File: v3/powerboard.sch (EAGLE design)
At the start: 4 parts, among them U1 TPS63001DRCR

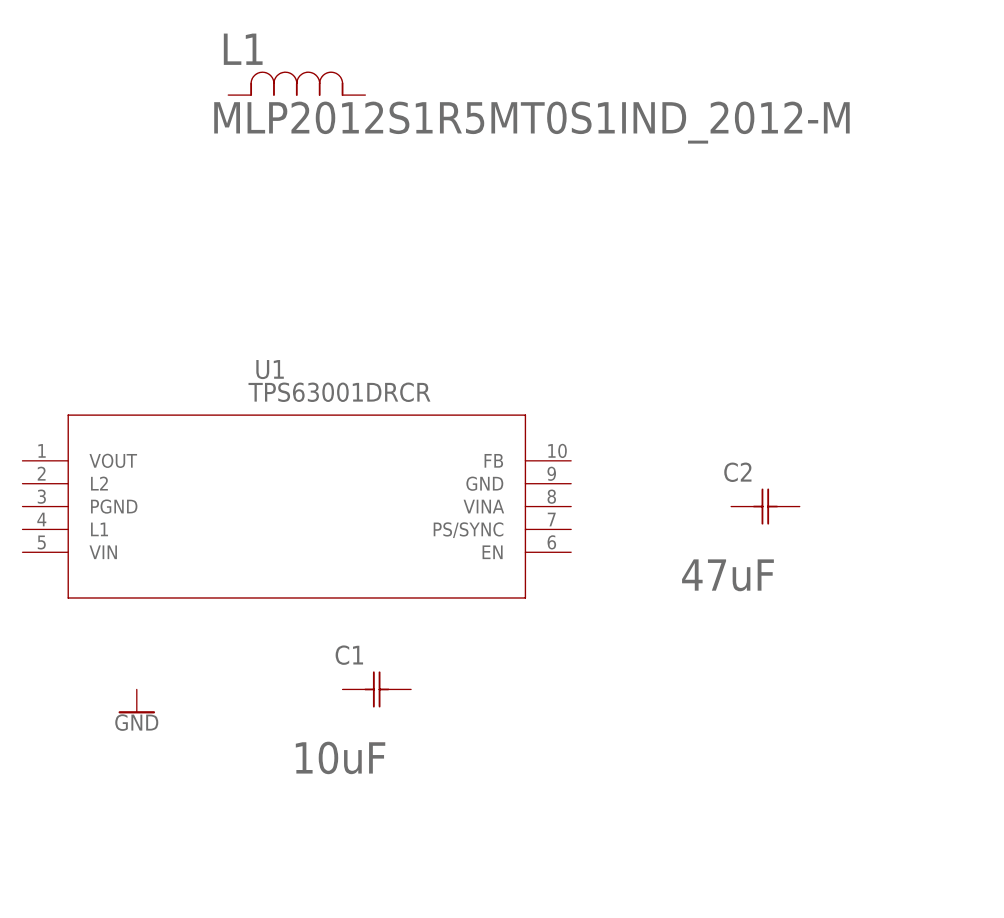
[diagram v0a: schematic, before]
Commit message: Progress on two-rail power supply.
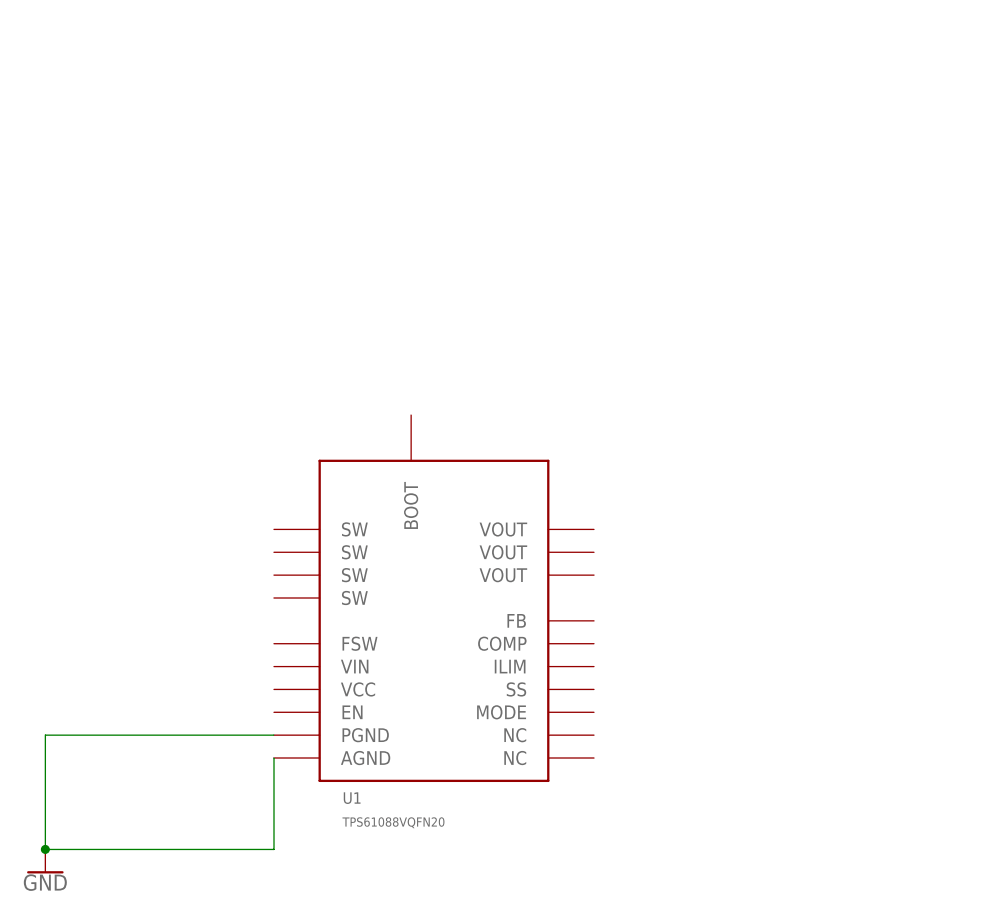
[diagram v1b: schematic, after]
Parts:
- removed C1: 10uF, Murata_By_element14_Batch_1:GRM188R60J106ME47D
- removed C2: 47uF, Murata_By_element14_Batch_1:GRM31MR71E105KA01L
- removed L1: MLP2012S1R5MT0S1IND_2012-M, digikey_2:MLP2012S1R5MT0S1IND_2012-M
- U1: value TPS63001DRCR -> TPS61088VQFN20; device digikey_2:TPS63001DRCR -> digikey:TPS61088VQFN20
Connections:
- new net GND: U1.AGND, U1.PGND
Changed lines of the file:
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@@
 </classes>
 <parts>
-<part name="L1" library="digikey_2" deviceset="MLP2012S1R5MT0S1" device="IND_2012-M"/>
-<part name="U1" library="digikey_2" deviceset="TPS63001DRCR" device=""/>
-<part name="C1" library="Murata_By_element14_Batch_1" deviceset="GRM188R60J106ME47D" device="" value="10uF"/>
-<part name="C2" library="Murata_By_element14_Batch_1" deviceset="GRM31MR71E105KA01L" device="" value="47uF"/>
 <part name="GND1" library="SparkFun-PowerSymbols" deviceset="GND" device=""/>
+<part name="U1" library="digikey" deviceset="TPS61088" device="VQFN20"/>
 </parts>
 <sheets>
@@
 </plain>
 <instances>
-<instance part="L1" gate="A" x="83.82" y="81.28"/>
-<instance part="U1" gate="A" x="58.42" y="40.64"/>
-<instance part="C1" gate="A" x="96.52" y="15.24"/>
-<instance part="C2" gate="A" x="139.7" y="35.56"/>
-<instance part="GND1" gate="1" x="73.66" y="12.7"/>
+<instance part="GND1" gate="1" x="63.5" y="-5.08"/>
+<instance part="U1" gate="G$1" x="106.68" y="27.94"/>
 </instances>
 <busses>
 </busses>
 <nets>
+<net name="GND" class="0">
+<segment>
+<pinref part="GND1" gate="1" pin="GND"/>
+<wire x1="63.5" y1="-2.54" x2="63.5" y2="10.16" width="0.1524" layer="91"/>
+<pinref part="U1" gate="G$1" pin="PGND"/>
+<wire x1="63.5" y1="10.16" x2="88.9" y2="10.16" width="0.1524" layer="91"/>
+<pinref part="U1" gate="G$1" pin="AGND"/>
+<wire x1="63.5" y1="-2.54" x2="88.9" y2="-2.54" width="0.1524" layer="91"/>
+<wire x1="88.9" y1="-2.54" x2="88.9" y2="7.62" width="0.1524" layer="91"/>
+<junction x="63.5" y="-2.54"/>
+</segment>
+</net>
 </nets>
 </sheet>

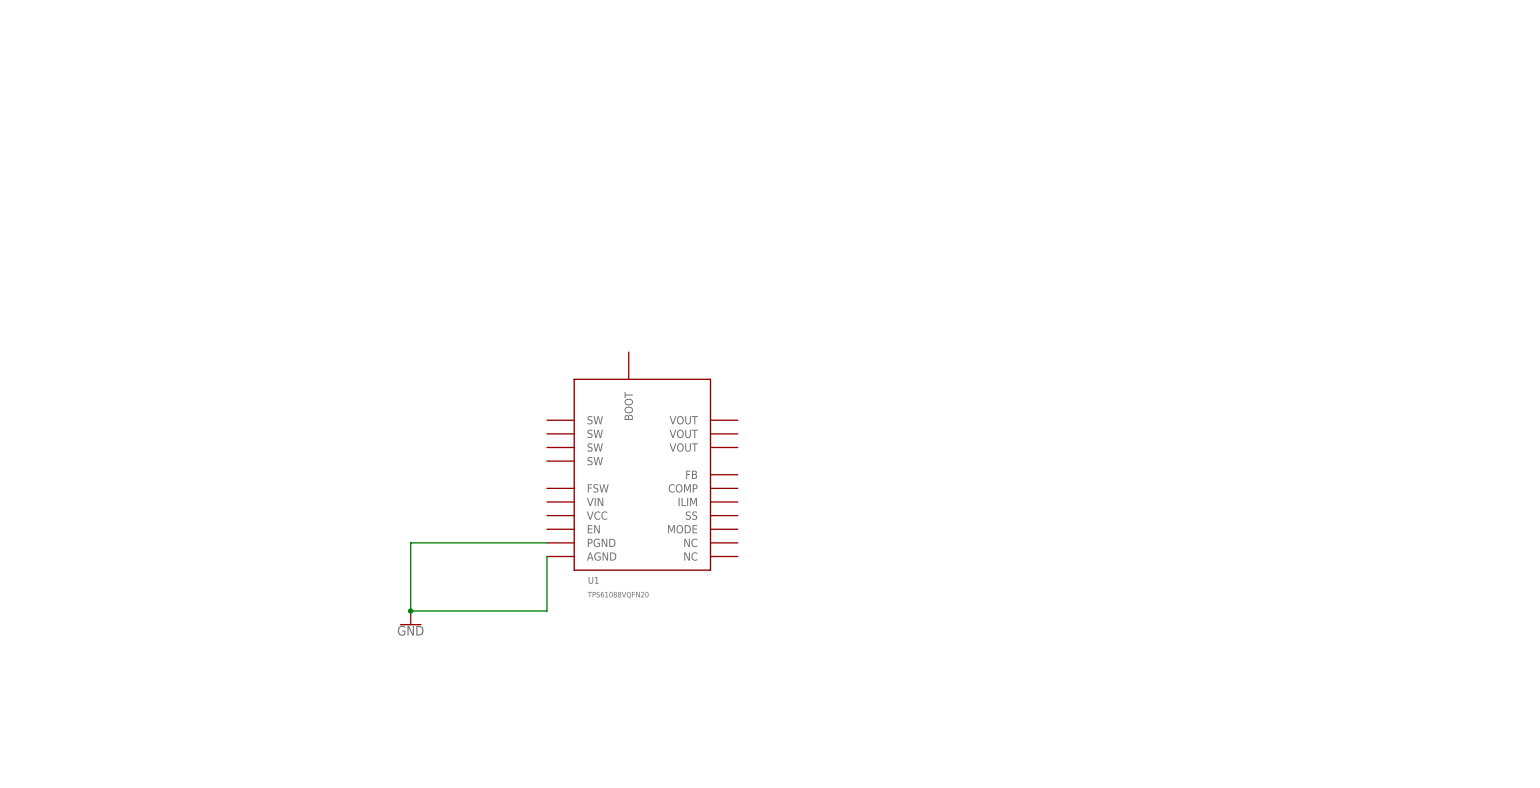
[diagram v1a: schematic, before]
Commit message: 6v schematic complete.
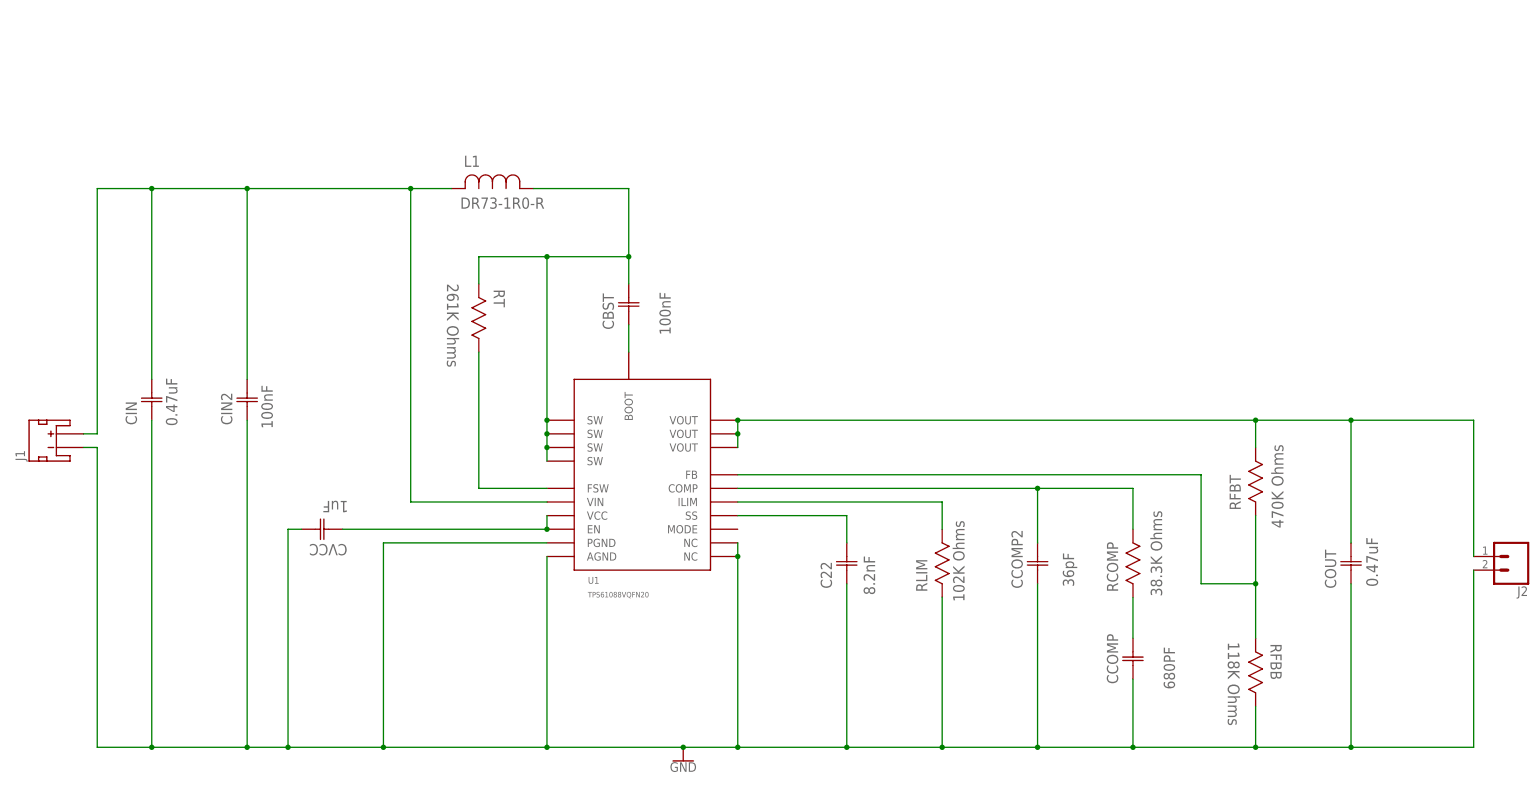
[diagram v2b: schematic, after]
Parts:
- added C22: 8.2nF, Kemet_By_element14_Batch_1:C0402C822K5RACTU
- added CBST: 100nF, AVX_By_element14_Batch_1:08053C104KAT2A
- added CCOMP: 680PF, AVX_By_element14_Batch_1:0603YC681JAT2A
- added CCOMP2: 36pF, Kemet_By_element14_Batch_1:C0402C360J5GACTU
- added CIN, COUT: 0.47uF, Kemet_By_element14_Batch_1:C1206F474K5RACAUTO
- added CIN2: 100nF, Murata_By_element14_Batch_1:GRM155R71C104KA88D
- added CVCC: 1uF, Murata_By_element14_Batch_1:GRM188R60J105KA01D
- added J1: (no value), SparkFun-Connectors:JST_2MM_MALE
- added J2: (no value), SparkFun-Connectors:CONN_02PTH3
- added L1: DR73-1R0-R, Coiltronics_By_element14_Batch_1:DR73-1R0-R
- added RCOMP: 38.3K Ohms, Vishay_By_element14_Batch_1:CRCW040238K3FKED
- added RFBB: 118K Ohms, Vishay_By_element14_Batch_1:CRCW0402118KFKED
- added RFBT: 470K Ohms, Yageo_By_element14_Batch_1:RC0603FR-07470KL
- added RLIM: 102K Ohms, Vishay_By_element14_Batch_1:CRCW0402102KFKED
- added RT: 261K Ohms, Vishay_By_element14_Batch_1:CRCW0402261KFKED
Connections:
- new net BOOT: CBST.C1, U1.BOOT
- new net COMP: CCOMP2.C2, RCOMP.1, U1.COMP
- new net ILIM: RLIM.1, U1.ILIM
- new net N$1: CCOMP.C2, RCOMP.2
- new net N$3: RT.1, U1.FSW
- new net N$4: RFBB.2, RFBT.R2, U1.FB
- new net SS: C22.C2, U1.SS
- new net SW: CBST.C2, L1.1, RT.2, U1.SW@4, U1.SW@5, U1.SW@6, U1.SW@7
- new net VCC: CVCC.C1, U1.EN, U1.VCC
- new net VIN: CIN.C2, CIN2.C2, J1.+, L1.2, U1.VIN
- new net VOUT: COUT.C2, J2.1, RFBT.R1, U1.VOUT@14, U1.VOUT@15, U1.VOUT@16
- net GND: now also C22.C1, CCOMP.C1, CCOMP2.C1, CIN.C1, CIN2.C1, COUT.C1, CVCC.C2, J1.-, J2.2, RFBB.1, RLIM.2, U1.NC@11, U1.NC@12

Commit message: Progress on 6v eval board.
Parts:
- J1: device SparkFun-Connectors:JST_2MM_MALE -> SparkFun-Connectors:CONN_06LONGPADS
- J2: device SparkFun-Connectors:CONN_02PTH3 -> SparkFun-Connectors:CONN_04LONGPADS
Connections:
- net N$3 renamed FSW
- net N$4 renamed FB
- new net EN: J1.3, U1.EN
- net GND: now also J1.2, J1.>NAME, J2.1, U1.PGND@21, U1.PGND@22, U1.PGND@23, U1.PGND@24; no longer J1.-, U1.PGND
- net VCC: no longer U1.EN
- net VIN: now also J1.4, J1.5, J1.6; no longer J1.+
- net VOUT: now also J2.3, J2.4; no longer J2.1
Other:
- moved on the sheet: CVCC

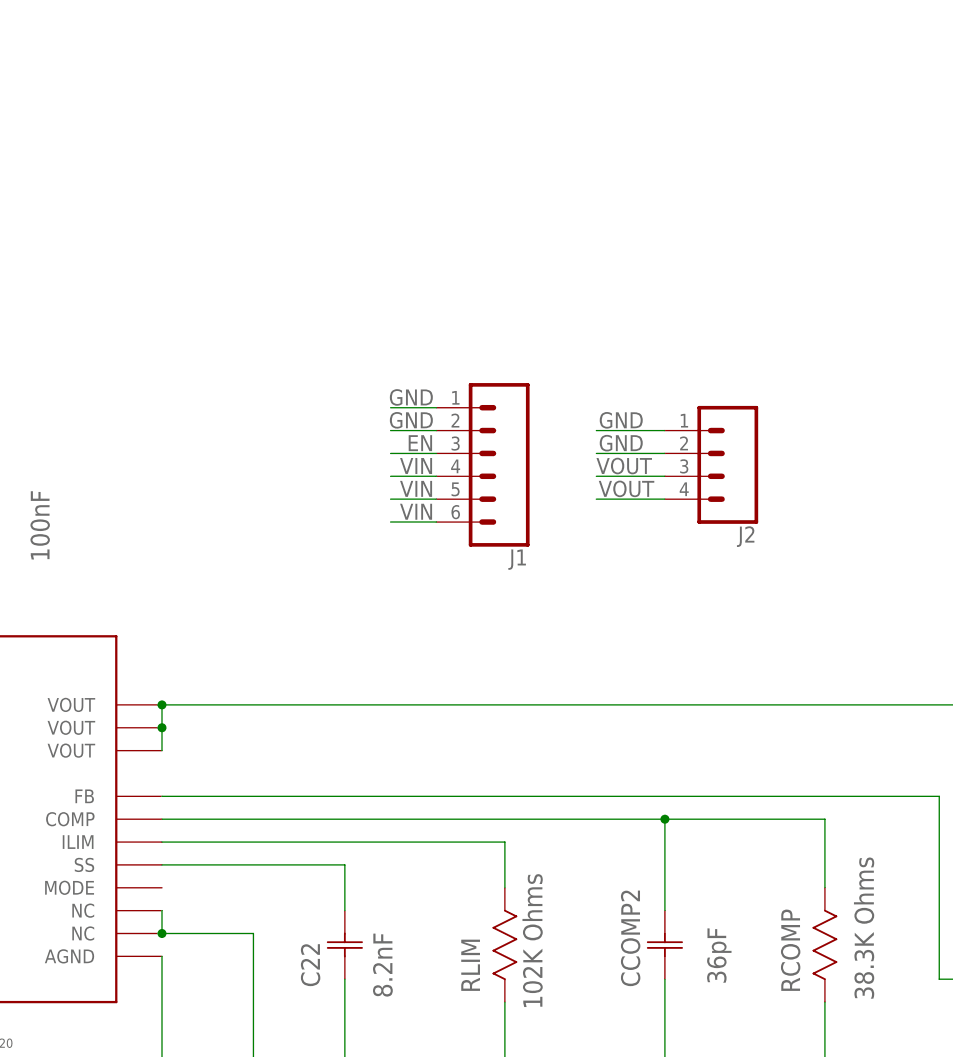
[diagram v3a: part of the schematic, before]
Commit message: Significant progress on layout for 6v eval.
TODO:
* bottom layer
* vias
* DRC errors in QFN part.
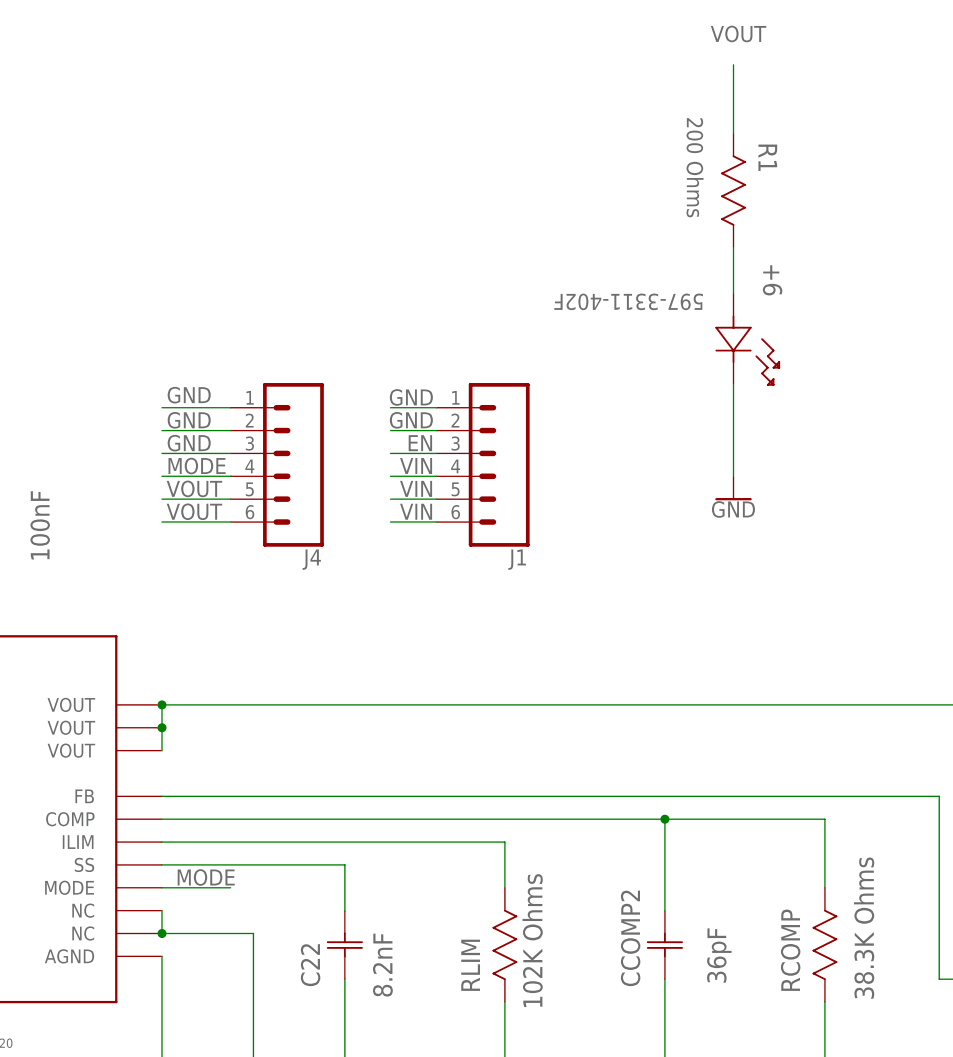
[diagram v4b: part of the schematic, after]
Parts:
- removed J2: (no value), SparkFun-Connectors:CONN_04LONGPADS
- added +6: 597-3311-402F, Dialight_By_element14_Batch_1:597-3311-402F
- added J4: (no value), SparkFun-Connectors:CONN_06LONGPADS
- added R1: 200 Ohms, Vishay_By_element14_Batch_1:CRCW1206200RJNEA
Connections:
- new net LED_ANODE: +6.2, R1.1
- new net MODE: J4.4, U1.MODE
- net GND: now also +6.1, J4.2, J4.3, J4.>NAME; no longer J2.1, J2.2
- net VOUT: now also J4.5, J4.6, R1.2; no longer J2.3, J2.4
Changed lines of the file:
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@@
 <part name="L1" library="Coiltronics_By_element14_Batch_1" deviceset="DR73-1R0-R" device=""/>
 <part name="J1" library="SparkFun-Connectors" deviceset="CONN_06" device="LONGPADS"/>
-<part name="J2" library="SparkFun-Connectors" deviceset="CONN_04" device="LONGPADS"/>
+<part name="J4" library="SparkFun-Connectors" deviceset="CONN_06" device="LONGPADS"/>
+<part name="+6" library="Dialight_By_element14_Batch_1" deviceset="597-3311-402F" device=""/>
+<part name="R1" library="Vishay_By_element14_Batch_1" deviceset="CRCW1206200RJNEA" device="" value="200 Ohms"/>
+<part name="GND2" library="SparkFun-PowerSymbols" deviceset="GND" device=""/>
 </parts>
 <sheets>
@@
 <instance part="L1" gate="A" x="71.12" y="76.2"/>
 <instance part="J1" gate="G$1" x="160.02" y="60.96" rot="R180"/>
-<instance part="J2" gate="G$1" x="185.42" y="60.96" rot="R180"/>
+<instance part="J4" gate="G$1" x="137.16" y="60.96" rot="R180"/>
+<instance part="+6" gate="A" x="187.96" y="78.74" smashed="yes" rot="R270">
+<attribute name="VALUE" x="184.7342" y="78.6892" size="1.778" layer="96" ratio="10" rot="SR180"/>
+<attribute name="NAME" x="191.262" y="82.1436" size="2.0828" layer="95" ratio="10" rot="SR270"/>
+</instance>
+<instance part="R1" gate="A" x="187.96" y="96.52" smashed="yes" rot="R270">
+<attribute name="VALUE" x="182.7784" y="98.3742" size="1.778" layer="96" ratio="10" rot="SR270"/>
+<attribute name="NAME" x="190.7286" y="95.5294" size="2.0828" layer="95" ratio="10" rot="SR270"/>
+</instance>
+<instance part="GND2" gate="1" x="187.96" y="55.88"/>
 </instances>
 <busses>
@@
 </segment>
 <segment>
-<pinref part="J2" gate="G$1" pin="1"/>
-<wire x1="180.34" y1="63.5" x2="172.72" y2="63.5" width="0.1524" layer="91"/>
-<label x="172.974" y="63.754" size="1.778" layer="95"/>
-</segment>
-<segment>
-<pinref part="J2" gate="G$1" pin="2"/>
-<wire x1="180.34" y1="60.96" x2="172.72" y2="60.96" width="0.1524" layer="91"/>
-<label x="172.974" y="61.214" size="1.778" layer="95"/>
+<pinref part="J4" gate="G$1" pin="&gt;NAME"/>
+<wire x1="132.08" y1="66.04" x2="124.46" y2="66.04" width="0.1524" layer="91"/>
+<label x="124.968" y="66.548" size="1.778" layer="95"/>
+</segment>
+<segment>
+<pinref part="J4" gate="G$1" pin="3"/>
+<wire x1="132.08" y1="60.96" x2="124.46" y2="60.96" width="0.1524" layer="91"/>
+<label x="124.968" y="61.214" size="1.778" layer="95"/>
+</segment>
+<segment>
+<pinref part="J4" gate="G$1" pin="2"/>
+<wire x1="132.08" y1="63.5" x2="124.46" y2="63.5" width="0.1524" layer="91"/>
+<label x="124.968" y="63.754" size="1.778" layer="95"/>
+</segment>
+<segment>
+<pinref part="+6" gate="A" pin="1"/>
+<pinref part="GND2" gate="1" pin="GND"/>
+<wire x1="187.96" y1="68.58" x2="187.96" y2="58.42" width="0.1524" layer="91"/>
 </segment>
 </net>
@@
 </segment>
 <segment>
-<pinref part="J2" gate="G$1" pin="3"/>
-<wire x1="180.34" y1="58.42" x2="172.72" y2="58.42" width="0.1524" layer="91"/>
-<label x="172.72" y="58.674" size="1.778" layer="95"/>
-</segment>
-<segment>
-<pinref part="J2" gate="G$1" pin="4"/>
-<wire x1="180.34" y1="55.88" x2="172.72" y2="55.88" width="0.1524" layer="91"/>
-<label x="172.974" y="56.134" size="1.778" layer="95"/>
+<pinref part="J4" gate="G$1" pin="5"/>
+<wire x1="132.08" y1="55.88" x2="124.46" y2="55.88" width="0.1524" layer="91"/>
+<label x="124.968" y="56.134" size="1.778" layer="95"/>
+</segment>
+<segment>
+<pinref part="J4" gate="G$1" pin="6"/>
+<wire x1="132.08" y1="53.34" x2="124.46" y2="53.34" width="0.1524" layer="91"/>
+<label x="124.968" y="53.594" size="1.778" layer="95"/>
+</segment>
+<segment>
+<pinref part="R1" gate="A" pin="2"/>
+<wire x1="187.96" y1="96.52" x2="187.96" y2="104.14" width="0.1524" layer="91"/>
+<label x="185.42" y="106.68" size="1.778" layer="95"/>
 </segment>
 </net>
@@
 </segment>
 </net>
+<net name="MODE" class="0">
+<segment>
+<pinref part="U1" gate="G$1" pin="MODE"/>
+<wire x1="124.46" y1="12.7" x2="132.08" y2="12.7" width="0.1524" layer="91"/>
+<label x="125.984" y="12.954" size="1.778" layer="95"/>
+</segment>
+<segment>
+<pinref part="J4" gate="G$1" pin="4"/>
+<wire x1="132.08" y1="58.42" x2="124.46" y2="58.42" width="0.1524" layer="91"/>
+<label x="124.968" y="58.674" size="1.778" layer="95"/>
+</segment>
+</net>
+<net name="LED_ANODE" class="0">
+<segment>
+<pinref part="+6" gate="A" pin="2"/>
+<pinref part="R1" gate="A" pin="1"/>
+<wire x1="187.96" y1="78.74" x2="187.96" y2="83.82" width="0.1524" layer="91"/>
+</segment>
+</net>
